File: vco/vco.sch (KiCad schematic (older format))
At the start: 41 parts

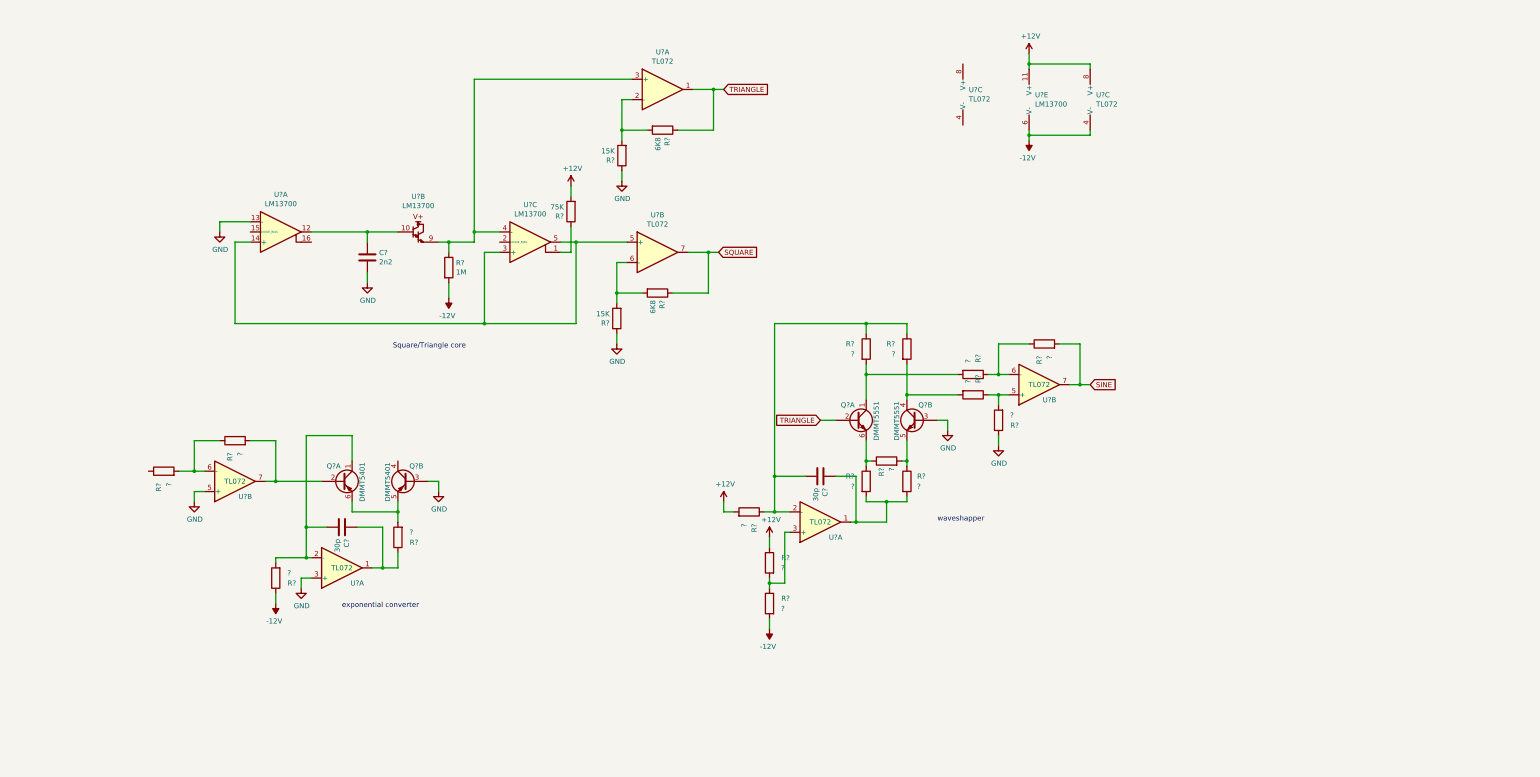
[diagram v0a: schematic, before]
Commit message: made progress on VCO
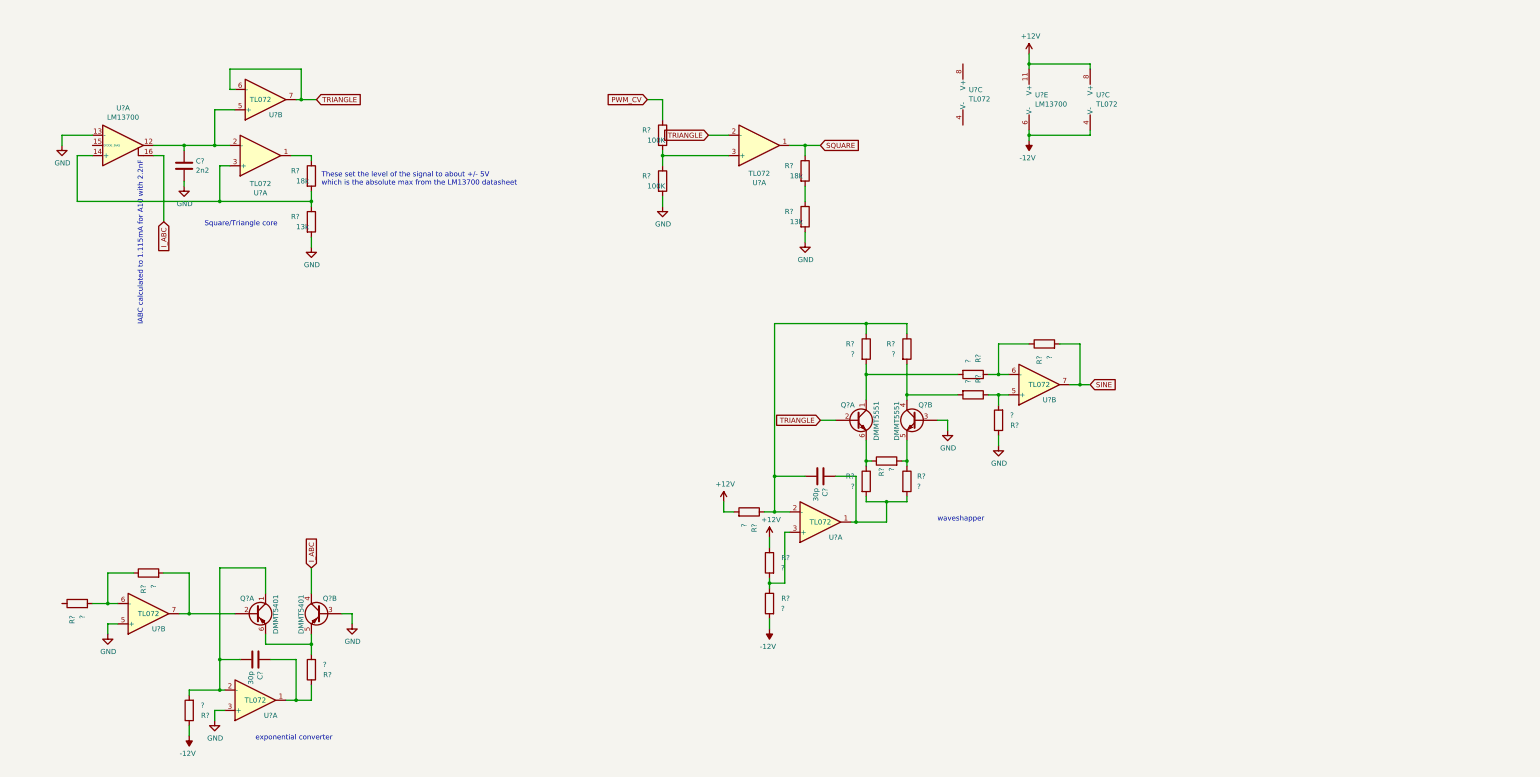
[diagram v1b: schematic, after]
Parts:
- removed R?: 1M, symbol Device:R
- removed R?: 75K, symbol Device:R
- removed R? (x2): 6K8, symbol Device:R
- removed R? (x2): 15K, symbol Device:R
- removed U? (x2): LM13700, symbol Amplifier_Operational:LM13700
- removed U?: TL072, symbol Amplifier_Operational:TL072
- added R? (x2): 18k, symbol Device:R
- added R? (x2): 13k, symbol Device:R
- added R? (x2): 100K, symbol Device:R
- added U? (x2): TL072, symbol Amplifier_Operational:TL072
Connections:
- net GND: now also R?.2, R?.2, R?.2
- net SQUARE: now also R?.1, U?.1
- net TRIANGLE: now also U?.2 (-), U?.6 (-), U?.7; no longer U?.1
- net at C?.1, U?.12: now also U?.2 (-), U?.5 (+)
- net at U?.14 (+): now also U?.3 (+), R?.1, R?.2
- net I_ABC: now reaches U?.16
- net I_ABC: now also Q?.4 (C2)
- new net: R?.1, U?.1
- new net: R?.1, R?.2, U?.3 (+)
- new net: R?.1, R?.2
- new net PWM_CV: R?.1
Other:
- note added: "IABC calculated to 1.115mA for A10 with 2.2nF"
- note added: "These set the level of the signal to about +/- 5V\nwhich is the absolute max from the LM13700 datasheet"
- moved on the sheet: C?, Q?A, Q?B, R?, U?A, U?B

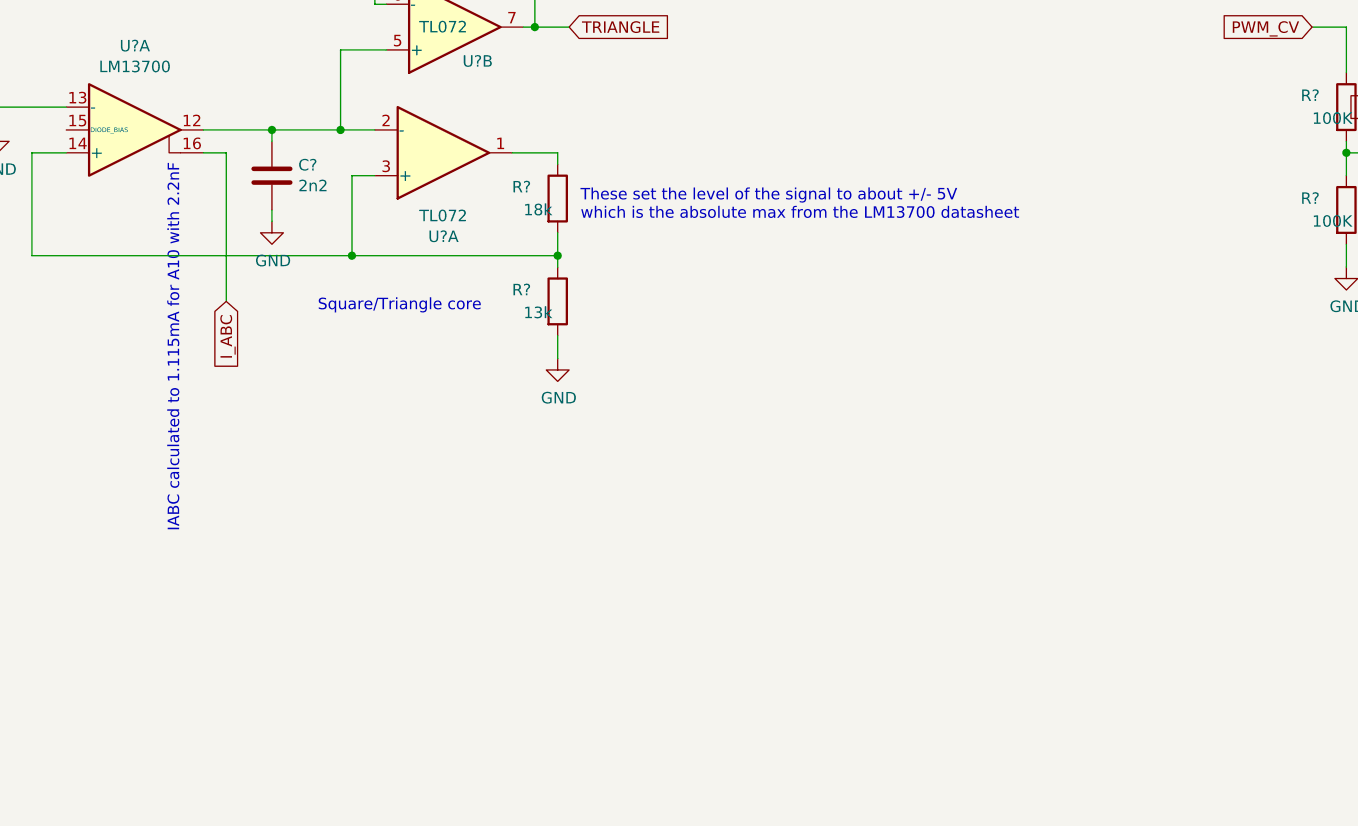
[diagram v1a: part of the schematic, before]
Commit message: it oscilates!
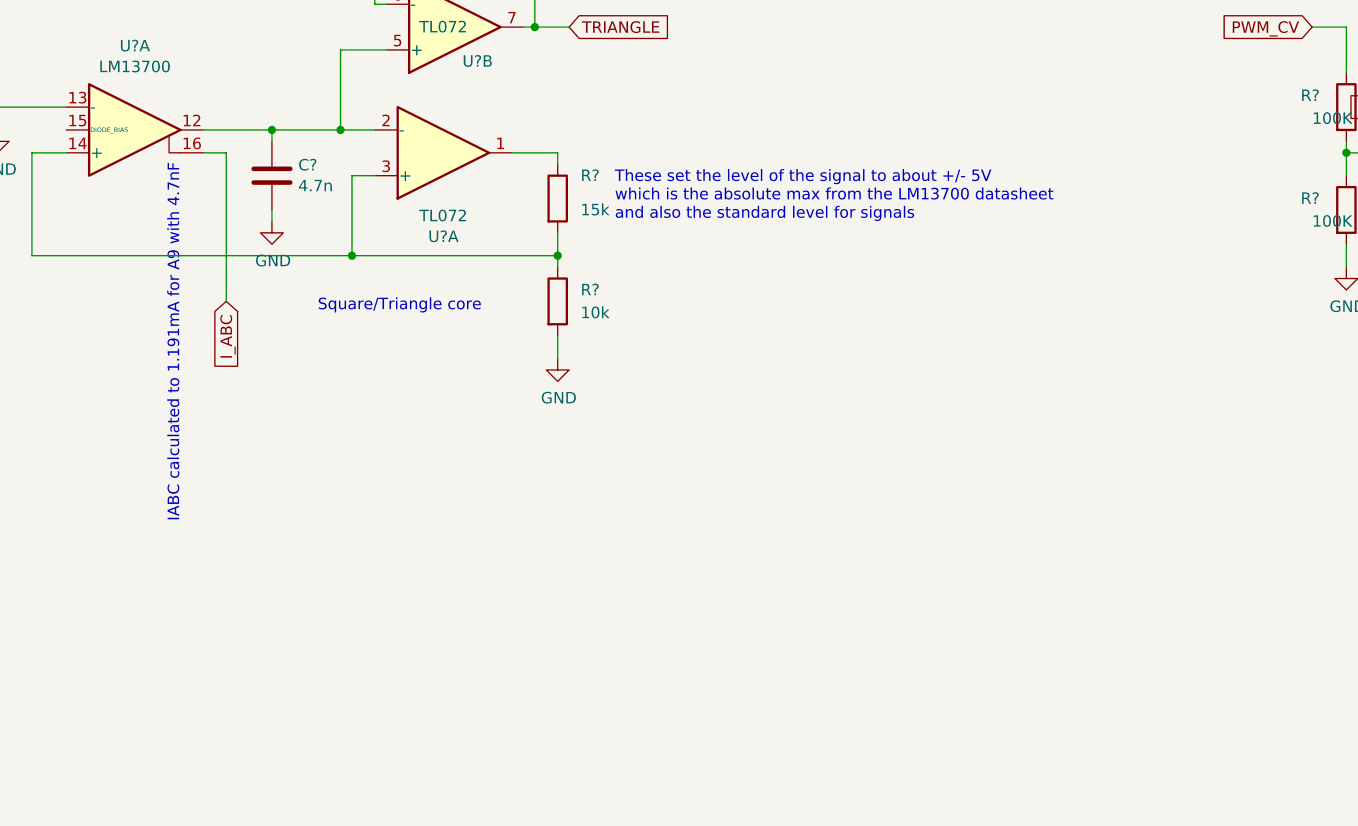
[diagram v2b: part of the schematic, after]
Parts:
- C?: value 2n2 -> 4.7n
- R?: value 18k -> 15k
- R?: value 13k -> 10k
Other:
- note added: "IABC calculated to 1.191mA for A9 with 4.7nF"
- note added: "These set the level of the signal to about +/- 5V\nwhich is the absolute max from the LM13700 datasheet\nand also the standard level for signals"
- note removed: "IABC calculated to 1.115mA for A10 with 2.2nF"
- note removed: "These set the level of the signal to about +/- 5V\nwhich is the absolute max from the LM13700 datasheet"
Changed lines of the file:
@@
 P 1900 1750
 F 0 "C?" H 2015 1796 50  0000 L CNN
-F 1 "2n2" H 2015 1705 50  0000 L CNN
+F 1 "4.7n" H 2015 1705 50  0000 L CNN
 F 2 "" H 1938 1600 50  0001 C CNN
 F 3 "~" H 1900 1750 50  0001 C CNN
@@
 U 1 1 5ED74B78
 P 3150 1850
-F 0 "R?" H 2950 1900 50  0000 L CNN
-F 1 "18k" H 3000 1800 50  0000 L CNN
+F 0 "R?" H 3250 1950 50  0000 L CNN
+F 1 "15k" H 3250 1800 50  0000 L CNN
 F 2 "" V 3080 1850 50  0001 C CNN
 F 3 "~" H 3150 1850 50  0001 C CNN
@@
 U 1 1 5ED74FEC
 P 3150 2300
-F 0 "R?" H 2950 2350 50  0000 L CNN
-F 1 "13k" H 3000 2250 50  0000 L CNN
+F 0 "R?" H 3250 2350 50  0000 L CNN
+F 1 "10k" H 3250 2250 50  0000 L CNN
 F 2 "" V 3080 2300 50  0001 C CNN
 F 3 "~" H 3150 2300 50  0001 C CNN
@@
 	1    0    0    -1
 $EndComp
-Text Notes 3250 1950 0    50   ~ 0
-These set the level of the signal to about +/- 5V\nwhich is the absolute max from the LM13700 datasheet
+Text Notes 3400 1950 0    50   ~ 0
+These set the level of the signal to about +/- 5V\nwhich is the absolute max from the LM13700 datasheet\nand also the standard level for signals
 $Comp
 L power:GND #PWR?
@@
 Connection ~ 2250 2100
 Text Notes 1500 1700 3    50   ~ 0
-IABC calculated to 1.115mA for A10 with 2.2nF
+IABC calculated to 1.191mA for A9 with 4.7nF
 Wire Wire Line
 	2400 1200 2200 1200

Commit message: vco planning
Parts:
- removed C?: 30p, symbol Device:C
- removed R? (x3): ?, symbol Device:R
- removed U?: TL072, symbol Amplifier_Operational:TL072
- added Q? (x2): DMMT5401, KiCad/kicad-footprints/Package_TO_SOT_SMD.pretty:SOT-23-6, symbol synth:DMMT5401
- added R?: ?, symbol Device:R
- added R? (x4): 10K, symbol Device:R
- added U?: TL072, symbol Amplifier_Operational:TL072
- added U?: ATtiny85V-10PU, Package_DIP:DIP-8_W7.62mm, symbol MCU_Microchip_ATtiny:ATtiny85V-10PU
- added U? (x4): 4066, symbol 4xxx:4066
- R?: value ? -> 12k
- R?: value 18k -> 15k
- R?: value 13k -> 10k
- R? (x2): value ? -> 68
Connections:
- net +12V: now also R?.1, R?.1; no longer R?.2
- net -12V: now also R?.2
- net GND: now also U?.5 (+), R?.2, R?.2, R?.2, R?.2, U?.4 (GND)
- net SINE: now also U?.8
- net SQUARE: now also R?.1, R?.2, U?.1; no longer R?.1, U?.1
- net TRIANGLE: now also R?.2, U?.4; no longer Q?.2 (B1)
- net at Q?.1 (C1): now also Q?.1 (C1), Q?.2 (B1), Q?.3 (B2); no longer R?.2
- net at R?.1, R?.1: now also R?.2; no longer Q?.6 (E1)
- net at Q?.4 (C2): now also R?.1, U?.6 (-), Q?.4 (C2); no longer R?.2
- net at Q?.5 (E2), R?.1: no longer R?.2
- net at R?.2: now also Q?.6 (E1); no longer R?.2
- net at R?.1, R?.2: now also U?.3 (+)
- new net: Q?.2 (B1), R?.2, U?.1
- new net: Q?.6 (E1), R?.2
- new net: Q?.5 (E2), R?.2
- new net: R?.1, R?.1, U?.2 (-)
- new net: R?.1, U?.1
- new net OUTPUT: U?.2, U?.3, U?.9
- new net SHAPE_CV: R?.1, U?.3 (XTAL2/PB4)
- new net SINE_EN: R?.1, U?.6, U?.7 (PB2)
- new net SQUARE_EN: R?.1, U?.13, U?.5 (AREF/PB0)
- new net TRIANGLE_EN: R?.1, U?.5, U?.6 (PB1)
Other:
- note added: "PWM control\nvia adjusting reference voltage of comparator"
- note added: "Rather than using a bunch of digital chips\nto convert an analog CV into a binned selector,\nprogramming a tiny uC requires only one IC and\nhas easy support for changing the bin size and\nadding hysteresis"
- note added: "TODO: one more output available if we can find a shape"
- note added: "TODO: protect against over/under voltage of shape cv"
- moved on the sheet: C?, Q?A, Q?B, R?, U?A, U?B
